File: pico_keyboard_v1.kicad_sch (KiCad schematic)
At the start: 15 parts, among them J1 Conn_01x04_12864, J2 Conn_01x03_Female, J3 Conn_01x03_Female, SW1 RotaryEncoder_Switch, U1 COM-09032, U2 Pico

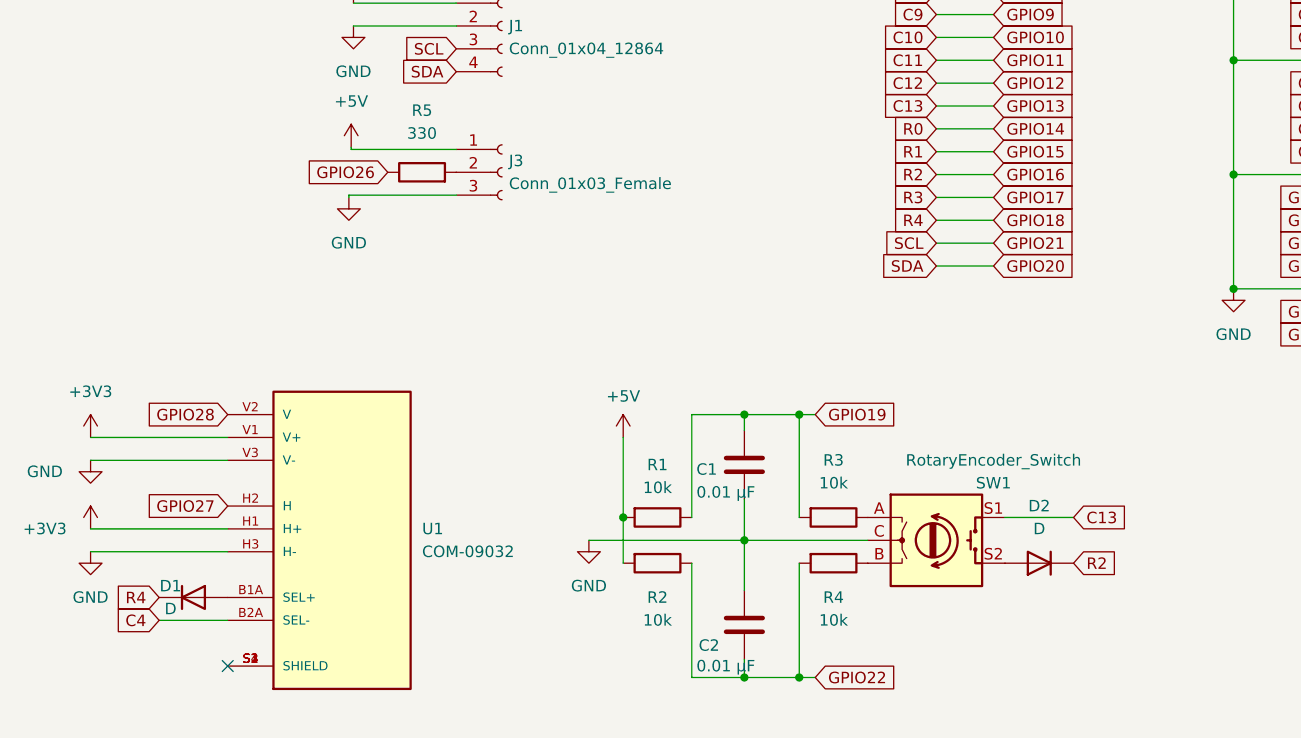
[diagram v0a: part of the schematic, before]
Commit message: Updated edge cut layer
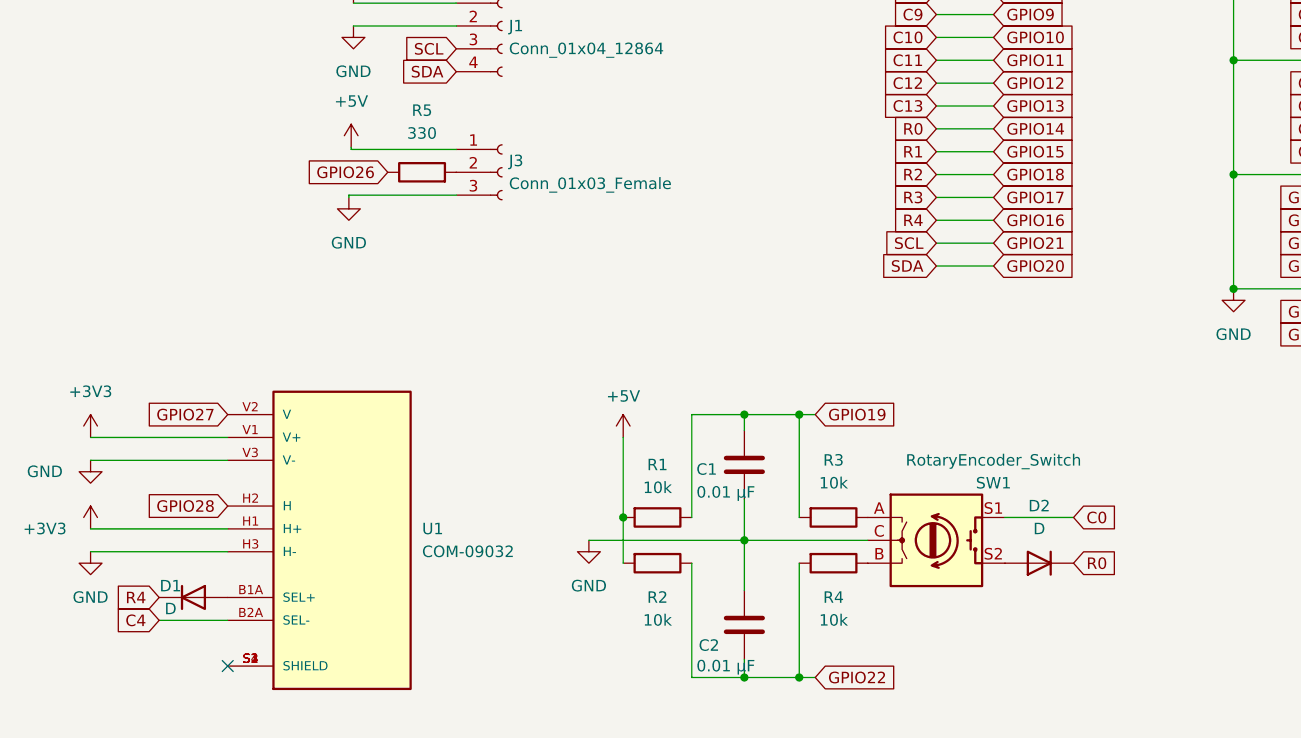
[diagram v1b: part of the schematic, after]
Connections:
- net C0: now also SW1.S1
- net C13: no longer SW1.S1
- net GPIO14: now also D2.1 (K)
- net GPIO16: now also D1.1 (K); no longer D2.1 (K)
- net GPIO18: no longer D1.1 (K)
- net GPIO27: now also U1.V2 (V); no longer U1.H2 (H)
- net GPIO28: now also U1.H2 (H); no longer U1.V2 (V)
